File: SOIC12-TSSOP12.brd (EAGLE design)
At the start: 20 x 17.8 mm, 7 parts

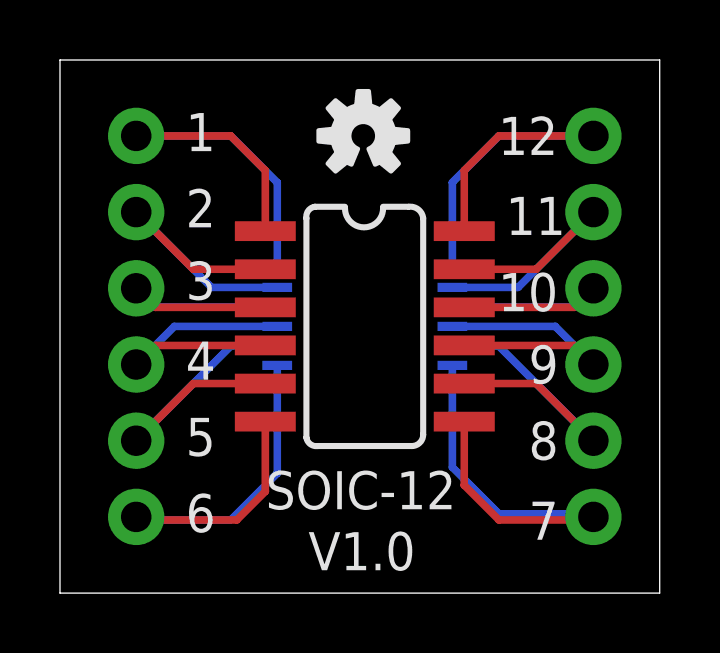
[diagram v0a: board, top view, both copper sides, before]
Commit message: Silk and board revision
Worked several silk screen issues and narrowed some boards.
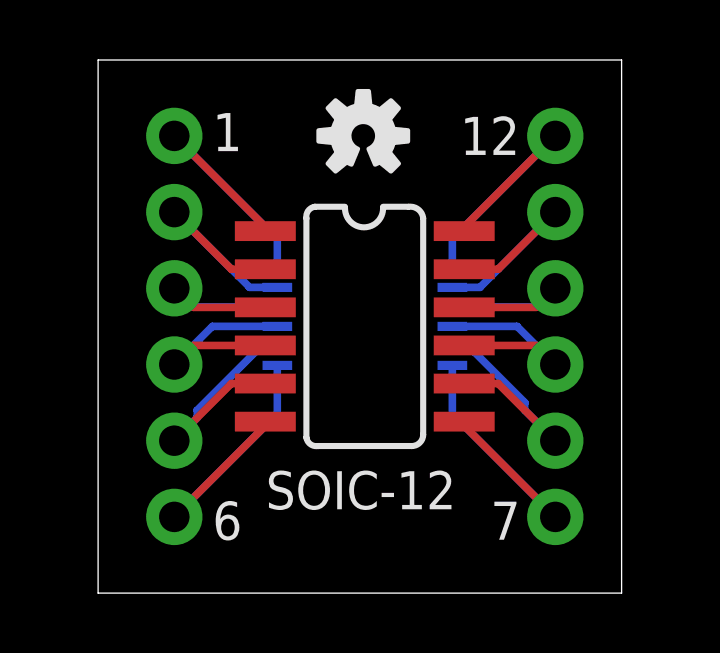
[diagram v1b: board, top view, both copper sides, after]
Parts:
- moved JP1 1.27 mm to (3.81, 12.7)
- moved JP2 1.27 mm to (16.5, 12.7)
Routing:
- net N$6: track 16.1 -> 10.9 mm
- net N$16: track 15.7 -> 10.9 mm
- net N$11: track 15.0 -> 10.3 mm
- net N$1: track 15.0 -> 10.3 mm
- net N$3: track 9.53 -> 6.99 mm
- net N$13: track 9.53 -> 6.99 mm
- net N$4: track 9.80 -> 7.26 mm
- net N$2: track 10.8 -> 8.30 mm
- net N$14: track 9.80 -> 7.26 mm
- net N$12: track 10.8 -> 8.30 mm
- net N$5: track 11.1 -> 8.71 mm
- net N$15: track 11.1 -> 8.71 mm
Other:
- board size 20 x 17.8 mm -> 17.4 x 17.8 mm
- board text removed: "10"
- board text removed: "3"
- board text removed: "4"
- board text removed: "5"
- board text removed: "8"
- board text removed: "9"
- board text removed: "V1.0"
